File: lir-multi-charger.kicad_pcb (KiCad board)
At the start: 2 copper layers, 90 x 58 mm, 13 parts, among them J1 Conn_01x02_Female, J11 Conn_01x01_Male, J12 Conn_01x01_Male

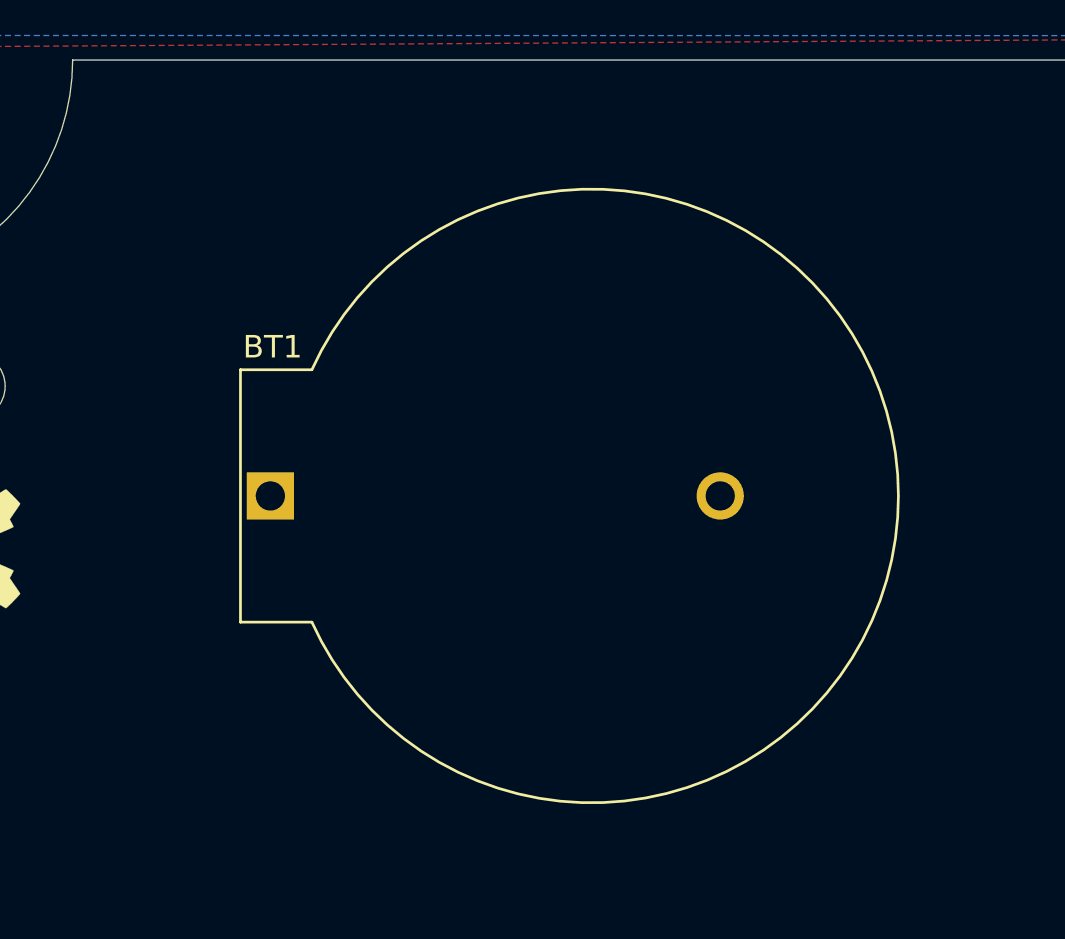
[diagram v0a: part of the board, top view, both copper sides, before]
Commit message: finished CR2450 battery holder footprint
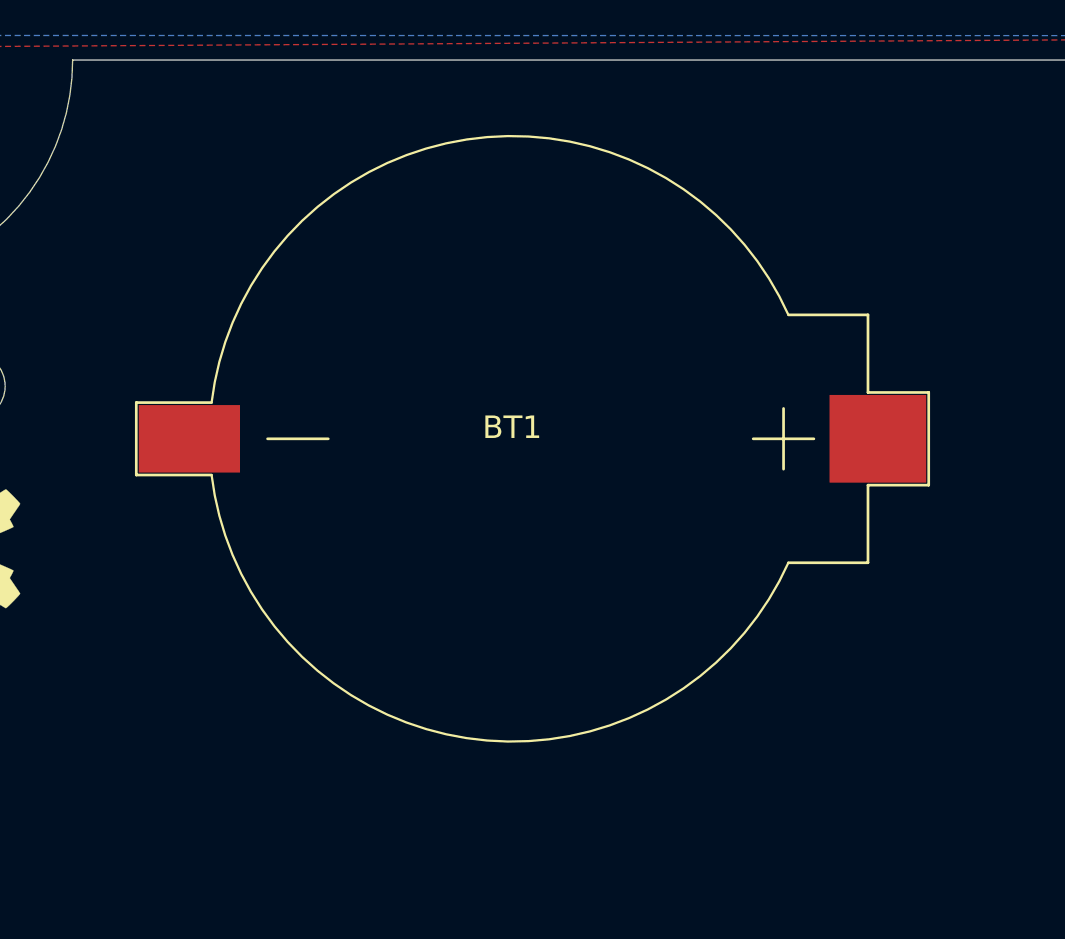
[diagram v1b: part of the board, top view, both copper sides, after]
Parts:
- BT1: footprint Battery:BatteryHolder_ComfortableElectronic_CH273-2450_1x2450 -> Battery_Coin_SMD:CR2450
- moved BT1 11.0 mm to (129.5, 116.8)
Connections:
- BT1 pad 1: unconnected-(BT1-Pad1) -> Net-(BT1-Pad1)
- J1 pad 1: unconnected-(J1-Pad1) -> Net-(BT1-Pad1)
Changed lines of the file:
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@@
   )
   (net 0 "")
-  (net 1 "unconnected-(J1-Pad1)")
+  (net 1 "Net-(BT1-Pad1)")
   (net 2 "unconnected-(J1-Pad2)")
-  (net 3 "unconnected-(BT1-Pad1)")
-  (net 4 "unconnected-(BT1-Pad2)")
-  (net 5 "Net-(J11-Pad1)")
+  (net 3 "unconnected-(BT1-Pad2)")
+  (net 4 "Net-(J11-Pad1)")
   (footprint "MountingHole:MountingHole_3mm" (layer "F.Cu")
     (at 105 129)
@@
     (fp_line (start 1.5 1.5) (end -1.5 1.5) (layer "F.CrtYd") (width 0.05))
     (pad "1" thru_hole circle locked (at 0 0) (size 1.99898 1.99898) (drill 0.8001) (layers *.Cu *.Mask)
-      (net 5 "Net-(J11-Pad1)"))
+      (net 4 "Net-(J11-Pad1)"))
   )
   (footprint "Connector_Wire:SolderWirePad_1x01_Drill0.8mm" (layer "F.Cu")
@@
     (fp_line (start 1.5 1.5) (end -1.5 1.5) (layer "F.CrtYd") (width 0.05))
     (pad "1" thru_hole circle locked (at 0 0) (size 1.99898 1.99898) (drill 0.8001) (layers *.Cu *.Mask)
-      (net 5 "Net-(J11-Pad1)"))
+      (net 4 "Net-(J11-Pad1)"))
   )
   (footprint "MountingHole:MountingHole_3mm" (layer "F.Cu")
@@
     (pad "" np_thru_hole circle locked (at 0 0) (size 3 3) (drill 3) (layers *.Cu *.Mask))
   )
-  (footprint "Battery:BatteryHolder_ComfortableElectronic_CH273-2450_1x2450" (layer "F.Cu")
-    (at 118.790914 119.38)
-    (descr "Comfortable Electronic CR2450 battery holder, http://www.comf.com.tw/ProductDetail.asp?no=148")
-    (tags "Comfortable Electronic CR2450")
+  (footprint "Battery_Coin_SMD:CR2450" (layer "F.Cu")
+    (at 129.54 116.84)
     (property "Sheetfile" "lir-multi-charger.kicad_sch")
     (property "Sheetname" "")
-    (attr through_hole)
-    (fp_text reference "BT1" (at 0.1 -6.62) (layer "F.SilkS")
-      (effects (font (size 1 1) (thickness 0.15)))
-    )
-    (fp_text value "Battery_Cell" (at 13.47 2.54) (layer "F.Fab")
-      (effects (font (size 1 1) (thickness 0.15)))
-    )
-    (fp_text user "${REFERENCE}" (at 14 0) (layer "F.Fab")
-      (effects (font (size 1 1) (thickness 0.1)))
-    )
-    (fp_line (start -1.33 5.61) (end -1.33 -5.61) (layer "F.SilkS") (width 0.12))
-    (fp_line (start -1.33 -5.61) (end 1.845 -5.61) (layer "F.SilkS") (width 0.12))
-    (fp_line (start 1.845 5.61) (end -1.33 5.61) (layer "F.SilkS") (width 0.12))
-    (fp_arc (start 1.845 -5.61) (mid 27.921896 0) (end 1.845 5.61) (layer "F.SilkS") (width 0.12))
-    (fp_line (start 1.77 5.75) (end -1.47 5.75) (layer "F.CrtYd") (width 0.05))
-    (fp_line (start -1.47 -5.75) (end 1.77 -5.75) (layer "F.CrtYd") (width 0.05))
-    (fp_line (start -1.47 5.75) (end -1.47 -5.75) (layer "F.CrtYd") (width 0.05))
-    (fp_arc (start 1.77 -5.75) (mid 28.048173 0) (end 1.77 5.75) (layer "F.CrtYd") (width 0.05))
-    (fp_line (start -1.22 5.5) (end -1.22 -5.5) (layer "F.Fab") (width 0.1))
-    (fp_line (start 1.95 5.5) (end -1.22 5.5) (layer "F.Fab") (width 0.1))
-    (fp_line (start -1.22 -5.5) (end 1.95 -5.5) (layer "F.Fab") (width 0.1))
-    (fp_arc (start 1.95 -5.5) (mid 27.78107 0) (end 1.95 5.5) (layer "F.Fab") (width 0.1))
-    (pad "1" thru_hole rect (at 0 0 270) (size 2.1 2.1) (drill 1.3) (layers *.Cu *.Mask)
-      (net 3 "unconnected-(BT1-Pad1)") (pinfunction "+") (pintype "passive"))
-    (pad "2" thru_hole circle (at 20 0 270) (size 2.1 2.1) (drill 1.3) (layers *.Cu *.Mask)
-      (net 4 "unconnected-(BT1-Pad2)") (pinfunction "-") (pintype "passive"))
-    (model "${KICAD6_3DMODEL_DIR}/Battery.3dshapes/BatteryHolder_ComfortableElectronic_CH273-2450_1x2450.wrl"
-      (offset (xyz 0 0 0))
-      (scale (xyz 1 1 1))
-      (rotate (xyz 0 0 0))
-    )
+    (attr smd)
+    (fp_text reference "BT1" (at 0 -0.5 unlocked) (layer "F.SilkS")
+      (effects (font (size 1 1) (thickness 0.15)))
+    )
+    (fp_text value "Battery_Cell" (at 0 1 unlocked) (layer "F.Fab")
+      (effects (font (size 1 1) (thickness 0.15)))
+    )
+    (fp_text user "${REFERENCE}" (at 0 2.5 unlocked) (layer "F.Fab")
+      (effects (font (size 1 1) (thickness 0.15)))
+    )
+    (fp_line (start -16.71 -1.61) (end -16.71 1.61) (layer "F.SilkS") (width 0.12))
+    (fp_line (start 10.715 0) (end 13.415 0) (layer "F.SilkS") (width 0.12))
+    (fp_line (start 15.819 -2.06) (end 18.519 -2.06) (layer "F.SilkS") (width 0.12))
+    (fp_line (start -16.71 -1.61) (end -13.363 -1.61) (layer "F.SilkS") (width 0.12))
+    (fp_line (start 15.819 2.06) (end 18.519 2.06) (layer "F.SilkS") (width 0.12))
+    (fp_line (start -16.71 1.61) (end -13.363 1.61) (layer "F.SilkS") (width 0.12))
+    (fp_line (start 15.819 -5.51) (end 15.819 -2.06) (layer "F.SilkS") (width 0.12))
+    (fp_line (start 12.281 5.51) (end 15.819 5.51) (layer "F.SilkS") (width 0.12))
+    (fp_line (start 18.519 -2.06) (end 18.519 2.06) (layer "F.SilkS") (width 0.12))
+    (fp_line (start 12.281 -5.51) (end 15.819 -5.51) (layer "F.SilkS") (width 0.12))
+    (fp_line (start 15.819 2.06) (end 15.819 5.51) (layer "F.SilkS") (width 0.12))
+    (fp_line (start 12.065 -1.35) (end 12.065 1.35) (layer "F.SilkS") (width 0.12))
+    (fp_line (start -10.875 0) (end -8.175 0) (layer "F.SilkS") (width 0.12))
+    (fp_arc (start 12.280364 5.51) (mid -2.023662 13.306742) (end -13.363 1.61) (layer "F.SilkS") (width 0.1))
+    (fp_arc (start -13.363 -1.61) (mid -2.023344 -13.306984) (end 12.281 -5.51) (layer "F.SilkS") (width 0.1))
+    (fp_line (start 18.659 -2.2) (end 18.659 2.2) (layer "F.CrtYd") (width 0.12))
+    (fp_line (start 15.959 -2.2) (end 18.659 -2.2) (layer "F.CrtYd") (width 0.12))
+    (fp_line (start -16.85 -1.75) (end -13.487 -1.75) (layer "F.CrtYd") (width 0.12))
+    (fp_line (start -16.85 -1.75) (end -16.85 1.75) (layer "F.CrtYd") (width 0.12))
+    (fp_line (start 15.959 -5.65) (end 15.959 -2.2) (layer "F.CrtYd") (width 0.12))
+    (fp_line (start 15.959 2.2) (end 15.959 5.65) (layer "F.CrtYd") (width 0.12))
+    (fp_line (start 15.959 2.2) (end 18.659 2.2) (layer "F.CrtYd") (width 0.12))
+    (fp_line (start -16.85 1.75) (end -13.487 1.75) (layer "F.CrtYd") (width 0.12))
+    (fp_line (start 12.371 -5.65) (end 15.959 -5.65) (layer "F.CrtYd") (width 0.12))
+    (fp_line (start 12.371 5.65) (end 15.959 5.65) (layer "F.CrtYd") (width 0.12))
+    (fp_arc (start 12.371 5.65) (mid -2.028231 13.448008) (end -13.487 1.75) (layer "F.CrtYd") (width 0.1))
+    (fp_arc (start -13.487 -1.75) (mid -2.028231 -13.448008) (end 12.371 -5.65) (layer "F.CrtYd") (width 0.1))
+    (fp_line (start 15.709 -5.4) (end 15.709 5.4) (layer "F.Fab") (width 0.12))
+    (fp_line (start 12.209 5.4) (end 15.709 5.4) (layer "F.Fab") (width 0.12))
+    (fp_line (start 12.209 -5.4) (end 15.709 -5.4) (layer "F.Fab") (width 0.12))
+    (fp_arc (start 12.209 5.4) (mid -13.350609 0) (end 12.209 -5.4) (layer "F.Fab") (width 0.1))
+    (pad "1" smd rect (at 16.259 0) (size 4.3 3.9) (layers "F.Cu" "F.Paste" "F.Mask")
+      (net 1 "Net-(BT1-Pad1)") (pinfunction "+") (pintype "passive"))
+    (pad "2" smd rect (at -14.35 0) (size 4.5 3) (layers "F.Cu" "F.Paste" "F.Mask")
+      (net 3 "unconnected-(BT1-Pad2)") (pinfunction "-") (pintype "passive"))
   )
   (footprint "TerminalBlock_4Ucon:TerminalBlock_4Ucon_1x02_P3.50mm_Horizontal" (layer "F.Cu")
@@
     (fp_circle (center 3.5 0) (end 4.875 0) (layer "F.Fab") (width 0.1) (fill none))
     (pad "1" thru_hole rect (at 0 0 90) (size 2.4 2.4) (drill 1.2) (layers *.Cu *.Mask)
-      (net 1 "unconnected-(J1-Pad1)") (pinfunction "Pin_1") (pintype "passive"))
+      (net 1 "Net-(BT1-Pad1)") (pinfunction "Pin_1") (pintype "passive"))
     (pad "2" thru_hole circle (at 3.5 0 90) (size 2.4 2.4) (drill 1.2) (layers *.Cu *.Mask)
       (net 2 "unconnected-(J1-Pad2)") (pinfunction "Pin_2") (pintype "passive"))
@@
     (effects (font (size 0.8 0.8) (thickness 0.15)))
   )
-  (zone (net 5) (net_name "Net-(J11-Pad1)") (layer "F.Cu") (hatch edge 0.508)
+  (zone (net 4) (net_name "Net-(J11-Pad1)") (layer "F.Cu") (hatch edge 0.508)
     (connect_pads (clearance 0.508))
     (min_thickness 0.254) (filled_areas_thickness no)
@@
     )
   )
-  (zone (net 5) (net_name "Net-(J11-Pad1)") (layer "B.Cu") (hatch edge 0.508)
+  (zone (net 4) (net_name "Net-(J11-Pad1)") (layer "B.Cu") (hatch edge 0.508)
     (connect_pads (clearance 0.508))
     (min_thickness 0.254) (filled_areas_thickness no)

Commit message: started charger schematic
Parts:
- added BT2: Battery_Cell, Battery_Coin_SMD:CR2032, F.Cu at (151.0, 135.2)
- added BT3: Battery_Cell, Battery_Coin_SMD:CR1220, F.Cu at (173.5, 137.6)
- added D1: D_Schottky, Diode_SMD:D_SOD-123, F.Cu at (176.5, 110.5)
- added D2: D_Schottky, Diode_SMD:D_SOD-123, F.Cu at (176.5, 114.3)
- added J2: Conn_01x02_Male, Connector_PinHeader_2.54mm:PinHeader_1x02_P2.54mm_Vertical, F.Cu at (177.8, 106.7)
- added R1: 5.1K, Resistor_SMD:R_0805_2012Metric_Pad1.20x1.40mm_HandSolder, F.Cu at (177.8, 118.1)
- added R2: 5.1K, Resistor_SMD:R_0805_2012Metric_Pad1.20x1.40mm_HandSolder, F.Cu at (174.9, 118.1)
- added U1: TP4056, Package_SO:SOP-8_3.9x4.9mm_P1.27mm, F.Cu at (151.1, 108.0)
- J1: value Conn_01x02_Female -> USB_C_Receptacle_USB2.0; footprint TerminalBlock_4Ucon:TerminalBlock_4Ucon_1x02_P3.50mm_Horizontal -> Connector_USB:USB_C_Receptacle_HRO_TYPE-C-31-M-12
- moved J12 16.7 mm to (185.4, 143.5)
- moved J11 15.8 mm to (185.4, 139.7)
- moved BT1 14.9 mm to (122.5, 130.0), turned to 90 degrees
- moved J1 5.90 mm to (185.4, 116.8)
- turned REF** to 0 degrees
- turned REF** to 180 degrees
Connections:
- BT1 pad 1: Net-(BT1-Pad1) -> unconnected-(BT1-Pad1)

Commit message: started placing components
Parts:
- added C1: 10uF, Capacitor_SMD:C_0805_2012Metric_Pad1.18x1.45mm_HandSolder, F.Cu at (157.5, 119.1)
- added C2: 10uF, Capacitor_SMD:C_0805_2012Metric_Pad1.18x1.45mm_HandSolder, F.Cu at (163.8, 124.5)
- added C3: 10uF, Capacitor_SMD:C_0805_2012Metric_Pad1.18x1.45mm_HandSolder, F.Cu at (140.5, 115.6)
- added C4: 10uF, Capacitor_SMD:C_0805_2012Metric_Pad1.18x1.45mm_HandSolder, F.Cu at (142.2, 121.9)
- added D3: GREEN, LED_SMD:LED_0805_2012Metric_Pad1.15x1.40mm_HandSolder, F.Cu at (178.5, 152.4)
- added D4: RED, LED_SMD:LED_0805_2012Metric_Pad1.15x1.40mm_HandSolder, F.Cu at (174.1, 152.1)
- added D5: GREEN, LED_SMD:LED_0805_2012Metric_Pad1.15x1.40mm_HandSolder, F.Cu at (157.5, 152.6)
- added D6: RED, LED_SMD:LED_0805_2012Metric_Pad1.15x1.40mm_HandSolder, F.Cu at (152.4, 152.4)
- added R10: 0R, Resistor_SMD:R_0805_2012Metric_Pad1.20x1.40mm_HandSolder, F.Cu at (149.6, 103.1)
- added R11: 320k, Resistor_SMD:R_0805_2012Metric_Pad1.20x1.40mm_HandSolder, F.Cu at (149.9, 107.0)
- added R12: 1R, Resistor_SMD:R_0805_2012Metric_Pad1.20x1.40mm_HandSolder, F.Cu at (149.9, 110.5)
- added R3: 1k, Resistor_SMD:R_0805_2012Metric_Pad1.20x1.40mm_HandSolder, F.Cu at (170.2, 118.4)
- added R4: 1k, Resistor_SMD:R_0805_2012Metric_Pad1.20x1.40mm_HandSolder, F.Cu at (170.2, 122.5)
- added R5: 0R, Resistor_SMD:R_0805_2012Metric_Pad1.20x1.40mm_HandSolder, F.Cu at (160.0, 102.9)
- added R6: 320k, Resistor_SMD:R_0805_2012Metric_Pad1.20x1.40mm_HandSolder, F.Cu at (160.0, 106.7)
- added R7: 1R, Resistor_SMD:R_0805_2012Metric_Pad1.20x1.40mm_HandSolder, F.Cu at (160.0, 110.5)
- added R8: 1k, Resistor_SMD:R_0805_2012Metric_Pad1.20x1.40mm_HandSolder, F.Cu at (153.8, 112.5)
- added R9: 1k, Resistor_SMD:R_0805_2012Metric_Pad1.20x1.40mm_HandSolder, F.Cu at (153.7, 117.1)
- added U2: TP4056, Li-ion-charger:tp4056, F.Cu at (147.3, 115.6)
- U1: footprint Package_SO:SOP-8_3.9x4.9mm_P1.27mm -> Li-ion-charger:tp4056
- moved U1 17.1 mm to (163.8, 119.4)
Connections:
- net Net-(D2-Pad1) renamed VBUS
- BT2 pad 1: unconnected-(BT2-Pad1) -> Net-(BT2-Pad1)
- BT2 pad 2: unconnected-(BT2-Pad2) -> GND
- BT3 pad 1: unconnected-(BT3-Pad1) -> Net-(U1-Pad5)
- BT3 pad 2: unconnected-(BT3-Pad2) -> GND
- U1 pad 1: unconnected-(U1-Pad1) -> GND
- U1 pad 2: unconnected-(U1-Pad2) -> Net-(U1-Pad2)
- U1 pad 3: unconnected-(U1-Pad3) -> GND
- U1 pad 4: unconnected-(U1-Pad4) -> Net-(C1-Pad1)
- U1 pad 5: unconnected-(U1-Pad5) -> Net-(U1-Pad5)
- U1 pad 6: unconnected-(U1-Pad6) -> Net-(U1-Pad6)
- U1 pad 7: unconnected-(U1-Pad7) -> Net-(U1-Pad7)
- U1 pad 8: unconnected-(U1-Pad8) -> Net-(C1-Pad1)

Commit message: placing components
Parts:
- added C5: 10uF, Capacitor_SMD:C_0805_2012Metric_Pad1.18x1.45mm_HandSolder, F.Cu at (137.2, 121.9)
- added C6: 10uF, Capacitor_SMD:C_0805_2012Metric_Pad1.18x1.45mm_HandSolder, F.Cu at (139.7, 127.0)
- added D7: GREEN, LED_SMD:LED_0805_2012Metric_Pad1.15x1.40mm_HandSolder, F.Cu at (134.6, 152.4)
- added D8: RED, LED_SMD:LED_0805_2012Metric_Pad1.15x1.40mm_HandSolder, F.Cu at (129.5, 152.4)
- added R13: 1k, Resistor_SMD:R_0805_2012Metric_Pad1.20x1.40mm_HandSolder, F.Cu at (135.1, 144.8)
- added R14: 1k, Resistor_SMD:R_0805_2012Metric_Pad1.20x1.40mm_HandSolder, F.Cu at (138.4, 144.8)
- added R15: 0R, Resistor_SMD:R_0805_2012Metric_Pad1.20x1.40mm_HandSolder, F.Cu at (139.7, 102.6)
- added R16: 320k, Resistor_SMD:R_0805_2012Metric_Pad1.20x1.40mm_HandSolder, F.Cu at (139.7, 106.7)
- added R17: 1R, Resistor_SMD:R_0805_2012Metric_Pad1.20x1.40mm_HandSolder, F.Cu at (139.7, 110.8)
- added U3: TP4056, Li-ion-charger:tp4056, F.Cu at (134.6, 115.6)
- moved R8 33.1 mm to (161.3, 144.8)
- moved R9 29.5 mm to (163.8, 144.8)
- moved R3 29.1 mm to (179.1, 146.1)
- moved R4 26.2 mm to (181.6, 146.1)
- moved J11 1.27 mm to (186.7, 139.7)
- moved J12 1.27 mm to (186.7, 143.5)
- moved C3 1.07 mm to (141.6, 115.6)
- moved C1 0.62 mm to (158.1, 119.1)
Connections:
- BT1 pad 1: unconnected-(BT1-Pad1) -> Net-(BT1-Pad1)
- BT1 pad 2: unconnected-(BT1-Pad2) -> GND

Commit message: all components placed
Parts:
- added J3: Conn_01x02_Male, Connector_PinHeader_2.54mm:PinHeader_1x02_P2.54mm_Vertical, F.Cu at (177.3, 121.9)
- added J4: Conn_01x02_Male, Connector_PinHeader_2.54mm:PinHeader_1x02_P2.54mm_Vertical, F.Cu at (156.5, 112.5)
- added J5: Conn_01x02_Male, Connector_PinHeader_2.54mm:PinHeader_1x02_P2.54mm_Vertical, F.Cu at (133.6, 107.4)
- added J6: Conn_01x02_Male, Connector_PinHeader_2.54mm:PinHeader_1x02_P2.54mm_Vertical, F.Cu at (177.8, 115.3)
- added JP1: SolderJumper_2_Bridged, Jumper:SolderJumper-2_P1.3mm_Bridged_RoundedPad1.0x1.5mm, F.Cu at (173.7, 122.9)
- added JP2: SolderJumper_2_Bridged, Jumper:SolderJumper-2_P1.3mm_Bridged_RoundedPad1.0x1.5mm, F.Cu at (153.1, 114.1)
- added JP3: SolderJumper_2_Bridged, Jumper:SolderJumper-2_P1.3mm_Bridged_RoundedPad1.0x1.5mm, F.Cu at (129.8, 108.5)
- moved D2 4.00 mm to (172.5, 114.3)
- moved R1 4.00 mm to (173.8, 118.1)
- moved R2 4.00 mm to (170.9, 118.1)
- moved D1 2.00 mm to (174.5, 110.5)
- moved R11 0.38 mm to (149.6, 106.7)
- moved D4 0.27 mm to (174.1, 152.4)
- moved R12 0.27 mm to (149.6, 110.5)
- moved R17 0.27 mm to (139.7, 110.5)
- moved R10 0.27 mm to (149.6, 102.9)
- moved R15 0.24 mm to (139.7, 102.9)
- moved D5 0.19 mm to (157.5, 152.4)
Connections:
- C2 pad 1: Net-(BT3-Pad1) -> Net-(C2-Pad1)
- C4 pad 1: Net-(BT2-Pad1) -> Net-(C4-Pad1)
- C6 pad 1: Net-(BT1-Pad1) -> Net-(C6-Pad1)
- U1 pad 5: Net-(BT3-Pad1) -> Net-(C2-Pad1)
- U2 pad 5: Net-(BT2-Pad1) -> Net-(C4-Pad1)
- U3 pad 5: Net-(BT1-Pad1) -> Net-(C6-Pad1)
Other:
- board text added: "D+"
- board text added: "D-"
- board text added: "GND"
- board text added: "LIR1220"
- board text added: "LIR2032"
- board text added: "LIR2450"
- board text added: "VCC"

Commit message: board routed
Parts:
- renumbered H2 to H0, H2 to H1, H3 to H2, H4 to H3, H6 to H5, H5 to H6, REF** to OSHW1, REF** to OSHW2
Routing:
- net GND: track 0.00 -> 278.2 mm
- net Net-(C1-Pad1): track 0.00 -> 75.8 mm, vias 0 -> 3
- net Net-(C5-Pad1): track 0.00 -> 67.0 mm
- net Net-(C3-Pad1): track 0.00 -> 66.6 mm, vias 0 -> 4
- net VBUS: track 0.00 -> 46.1 mm
- net Net-(R9-Pad2): track 0.00 -> 35.4 mm
- net Net-(R4-Pad2): track 0.00 -> 34.7 mm
- net Net-(R8-Pad2): track 0.00 -> 33.7 mm, vias 0 -> 2
- net Net-(R3-Pad2): track 0.00 -> 31.7 mm
- net Net-(R13-Pad2): track 0.00 -> 31.1 mm, vias 0 -> 2
- net Net-(R14-Pad2): track 0.00 -> 28.8 mm, vias 0 -> 2
- net Net-(C6-Pad1): track 0.00 -> 26.7 mm, vias 0 -> 2
- net Net-(C4-Pad1): track 0.00 -> 22.8 mm, vias 0 -> 1
- net Net-(C2-Pad1): track 0.00 -> 18.7 mm, vias 0 -> 1
- net Net-(R16-Pad1): track 0.00 -> 17.7 mm, vias 0 -> 2
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
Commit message: single gerber
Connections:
- J11 pad 1: Net-(J11-Pad1) -> GND
- J12 pad 1: Net-(J11-Pad1) -> GND
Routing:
- net GND: track 278.2 -> 334.8 mm
- net Net-(C1-Pad1): track 75.8 -> 76.4 mm
- net Net-(C5-Pad1): track 67.0 -> 67.5 mm
- added copper zone on B.Cu, net GND
- added copper zone on F.Cu, net GND
- removed copper zone on B.Cu, net Net-(J11-Pad1)
- removed copper zone on F.Cu, net Net-(J11-Pad1)
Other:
- rule pad_to_mask_clearance: 0.051 -> 0
